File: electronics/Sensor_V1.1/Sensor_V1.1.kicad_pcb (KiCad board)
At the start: 2 copper layers, 45.9 x 25.6 mm, 55 parts, among them J1 nuclone_small_left, J2 nuclone_small_right, J5 DevBoardUartInput, Q1 BC846, U1 PPG_sensor, U2 reference_sot23-3, U3 MCP6541

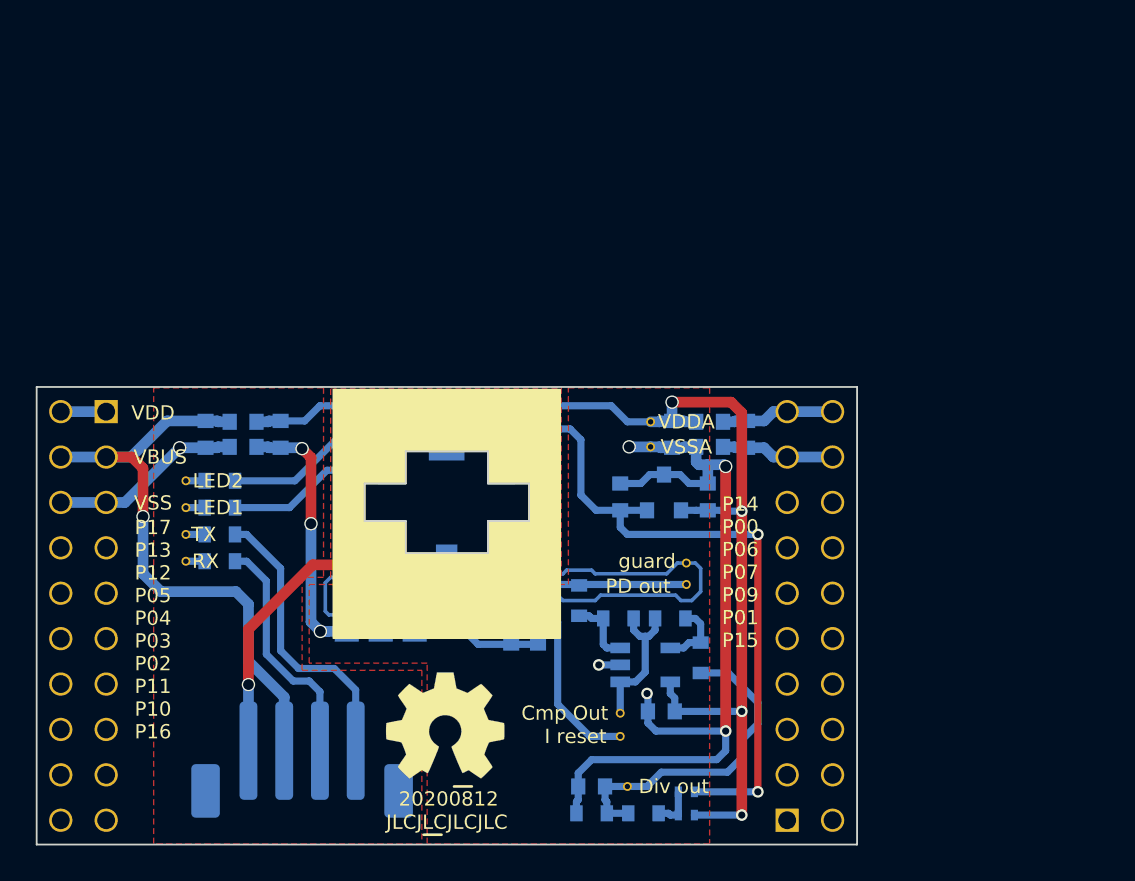
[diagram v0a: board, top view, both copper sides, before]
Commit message: minor layout changes and component swaps
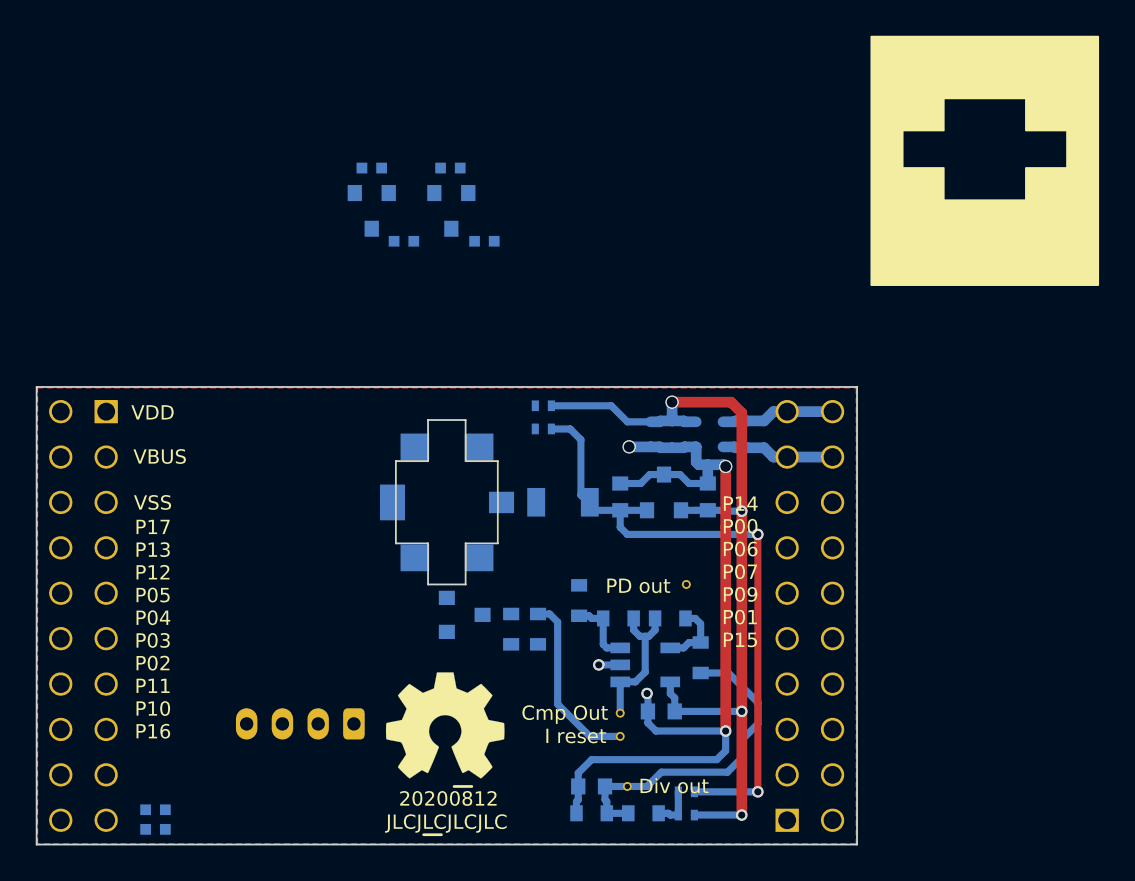
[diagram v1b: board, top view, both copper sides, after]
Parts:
- removed C1, C3: 1u, SquantorRcl:C_0603
- removed C2, C4: 10u, SquantorRcl:C_0603
- removed C7, C8: 4n7, SquantorRcl:C_0805+0603
- removed FB1, FB2, FB3, FB4: 600, SquantorRcl:L_0603
- removed JP2: bias VBUS, SquantorSpecial:solder_jumper_2way_noconn
- removed TP1: RX, SquantorTestPoints:TestPoint_hole_H03R05
- removed TP2: TX, SquantorTestPoints:TestPoint_hole_H03R05
- removed TP3: LED1, SquantorTestPoints:TestPoint_hole_H03R05
- removed TP4: LED2, SquantorTestPoints:TestPoint_hole_H03R05
- removed TP5, TP6: guard, SquantorTestPoints:TestPoint_pad_circle_D05
- removed TP7: VDDA, SquantorTestPoints:TestPoint_hole_H03R05
- removed TP8: VSSA, SquantorTestPoints:TestPoint_hole_H03R05
- removed TP9: guard, SquantorTestPoints:TestPoint_hole_H03R05
- added Q2: DMG1012, SquantorIC:SOT23-3, B.Cu at (80.9, 63.7)
- added Q3: DMG1012, SquantorIC:SOT23-3, B.Cu at (85.3, 63.7)
- added R5: 10K, SquantorRcl:R_0402_hand, B.Cu at (80.9, 61.3)
- added R6: 10K, SquantorRcl:R_0402_hand, B.Cu at (85.3, 61.3)
- C9: footprint SquantorRcl:C_0805+0603 -> SquantorRcl:C_1206
- J5: footprint Connector_JST:JST_PH_B4B-PH-SM4-TB_1x04-1MP_P2.00mm_Vertical -> Connector_JST:JST_PH_S4B-PH-K_1x04_P2.00mm_Horizontal
- R1, R2, R3, R4: footprint SquantorRcl:R_0603_hand -> SquantorRcl:R_0402_hand
- moved R4 20.0 mm to (87.2, 65.4)
- moved R3 18.1 mm to (82.7, 65.4)
- moved R2 15.8 mm to (68.8, 97.2)
- moved R1 15.4 mm to (68.8, 98.3)
- moved C9 10.4 mm to (91.6, 80.0), turned to 0 degrees
- moved J5 3.52 mm to (79.9, 92.4), turned to 180 degrees
- turned U1 to 0 degrees
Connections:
- net /GPIO_02 renamed Net-(J1-Pad9)
- net /GPIO_03 renamed Net-(J1-Pad10)
- net /GPIO_04 renamed Net-(J1-Pad11)
- net /GPIO_05 renamed Net-(J1-Pad12)
- net /GPIO_06 renamed Net-(J1-Pad13)
- net /GPIO_07 renamed Net-(J1-Pad14)
- net /GPIO_08 renamed Net-(J1-Pad15)
- net /GPIO_09 renamed Net-(J1-Pad16)
- net /GPIO_10 renamed Net-(J1-Pad17)
- net /GPIO_11 renamed Net-(J1-Pad18)
- net /GPIO_14 renamed Net-(J2-Pad1)
- net /GPIO_15 renamed Net-(J2-Pad2)
- net /GPIO_16 renamed Net-(J2-Pad3)
- net /GPIO_17 renamed Net-(J2-Pad4)
- net /GPIO_18 renamed Net-(J2-Pad5)
- net /GPIO_19 renamed Net-(J2-Pad6)
- net /GPIO_20 renamed Net-(J2-Pad7)
- net /GPIO_21 renamed Net-(J2-Pad8)
- net /GPIO_22 renamed Net-(J2-Pad9)
- net /GPIO_23 renamed Net-(J2-Pad10)
- net /GPIO_24 renamed Net-(J2-Pad11)
- net /GPIO_25 renamed Net-(J2-Pad12)
- net /GPIO_26 renamed Net-(J2-Pad13)
- net /GPIO_27 renamed Net-(J2-Pad14)
- net /GPIO_28 renamed Net-(J2-Pad15)
- net /GPIO_29 renamed Net-(J2-Pad16)
- C5 pad 1: /VDDA -> /VDD
- C5 pad 2: /VSSA -> /VSS
- C6 pad 2: /VSSA -> /VSS
- J1 pad 19: /GPIO_12 -> /UART_TX
- J1 pad 20: /GPIO_13 -> /UART_RX
- J1 pad 7: /GPIO_00 -> /LED1_EN
- J1 pad 8: /GPIO_01 -> /LED2_EN
- J2 pad 17: /VSSA_RAW -> /VSS
- J2 pad 18: /VSSA_RAW -> /VSS
- J2 pad 19: /VDDA_RAW -> /VDD
- J2 pad 20: /VDDA_RAW -> /VDD
- JP1 pad 1: /VDDA -> /VDD
- U1 pad 1: /LED1 -> /VDD
- U1 pad 3: /LED2 -> /VDD
- U1 pad 4: /VSS -> /LED2
- U1 pad 6: /VSS -> /LED1
- U2 pad 1: /VDDA -> /VDD
- U2 pad 3: /VSSA -> /VSS
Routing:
- net /PD_OUT_GUARD: track 45.2 -> 0.00 mm
- net /VBUS: track 34.2 -> 0.00 mm, vias 1 -> 0
- net /VSS: track 29.8 -> 6.37 mm, vias 4 -> 0
- net /PD_OUT: track 21.7 -> 0.00 mm
- net /VSSA: track 68.5 -> 47.1 mm, vias 9 -> 5
- net /LED2: track 18.3 -> 0.00 mm, vias 2 -> 0
- net Net-(J5-Pad4): track 16.4 -> 0.00 mm
- net Net-(J5-Pad3): track 13.5 -> 0.00 mm
- net /PD_BIAS: track 13.2 -> 0.00 mm
- net /LED1: track 9.61 -> 0.00 mm
- net /VSSA_RAW: track 6.37 -> 0.00 mm
- net /VDDA_RAW: track 6.37 -> 0.00 mm
- net Net-(Q1-Pad1): track 5.39 -> 0.00 mm
- net Net-(C4-Pad1): track 5.37 -> 0.00 mm
- net /VDD: track 2.54 -> 6.37 mm
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- removed copper zone on F.Cu, net /VSSA
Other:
- outline, holes or cut-outs redrawn

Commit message: updated versionnumber
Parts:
- N2: value 20200812 -> 20200908
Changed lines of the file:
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@@
       (effects (font (size 1 1) (thickness 0.15)))
     )
-    (fp_text value 20200812 (at 0.8 -0.1) (layer F.SilkS)
+    (fp_text value 20200908 (at 0.8 -0.1) (layer F.SilkS)
       (effects (font (size 0.8 0.8) (thickness 0.15)))
     )

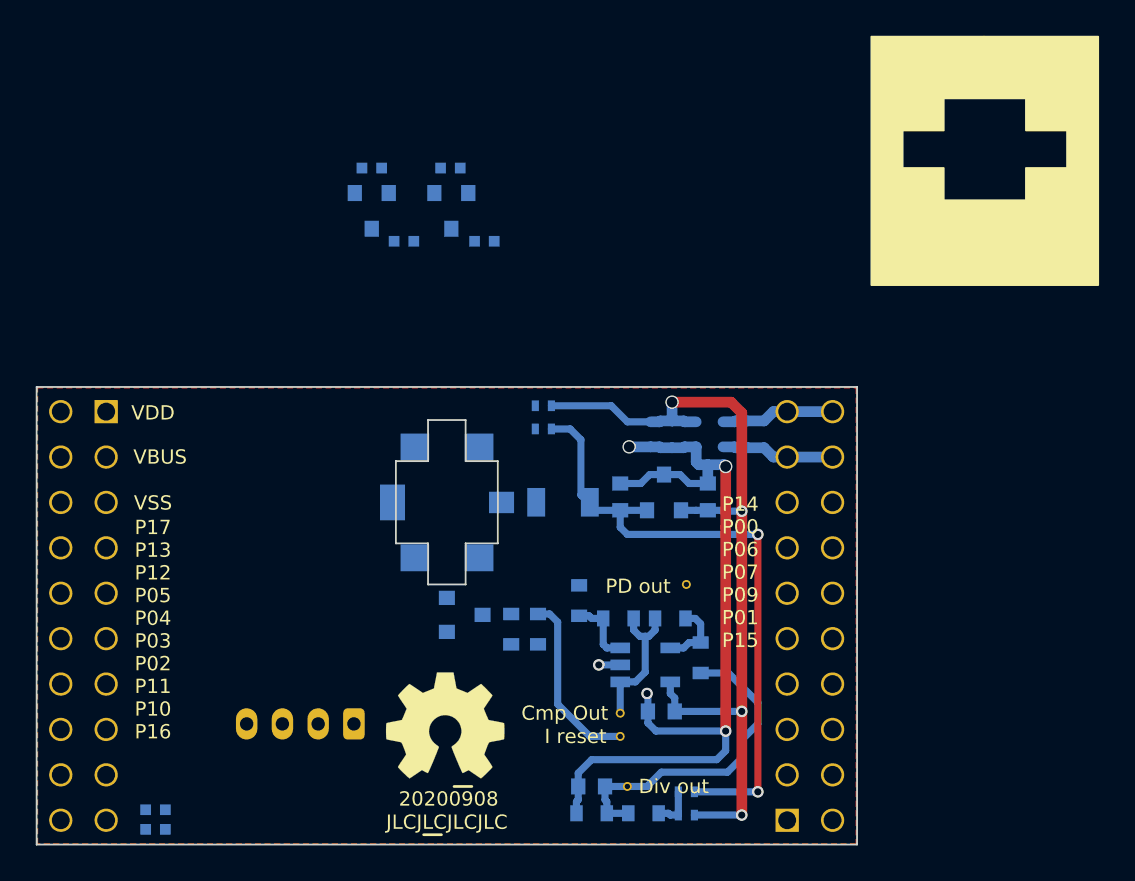
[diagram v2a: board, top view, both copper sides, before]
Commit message: placement and some routing of led drive circuitry
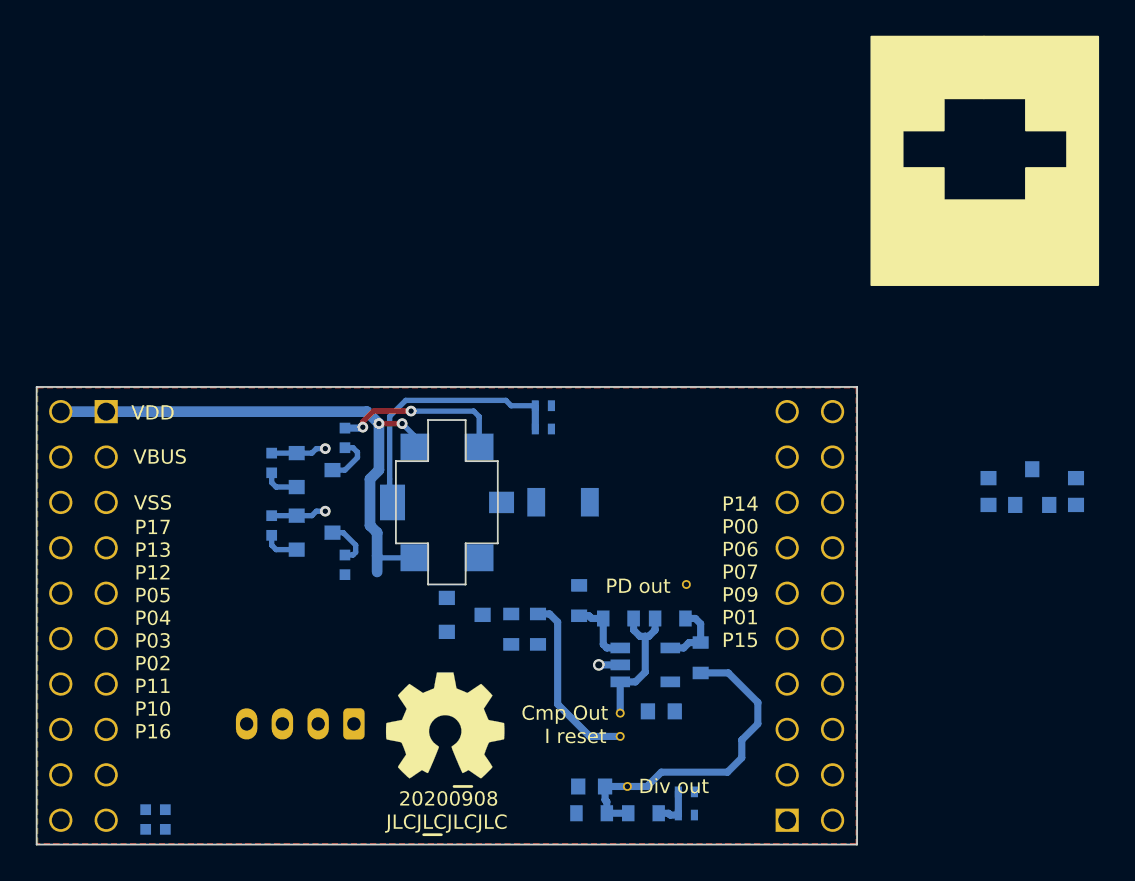
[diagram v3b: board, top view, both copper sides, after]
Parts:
- moved R5 20.8 mm to (75.3, 81.3), turned to 270 degrees
- moved C6 20.6 mm to (115.4, 79.4)
- moved C5 20.6 mm to (120.3, 79.4)
- moved U2 20.6 mm to (117.8, 79.2)
- moved R6 19.3 mm to (75.3, 77.8), turned to 270 degrees
- moved R3 18.4 mm to (79.4, 83.5), turned to 90 degrees
- moved Q2 18.3 mm to (77.7, 81.7), turned to 90 degrees
- moved Q3 16.4 mm to (77.7, 78.2), turned to 90 degrees
- moved R4 13.5 mm to (79.4, 76.4), turned to 270 degrees
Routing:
- net /VDDA: track 47.8 -> 0.00 mm, vias 4 -> 0
- net /VSSA: track 47.1 -> 1.20 mm, vias 5 -> 1
- net /VREF: track 35.8 -> 0.00 mm, vias 2 -> 0
- net /VDD: track 6.37 -> 31.8 mm, vias 0 -> 2
- net /PD_BIAS: track 0.00 -> 14.0 mm
- net /LED2: track 0.00 -> 9.91 mm, vias 0 -> 2
- net Net-(Q3-Pad3): track 0.00 -> 2.79 mm
- net Net-(Q2-Pad3): track 0.00 -> 2.65 mm
- net /LED2_EN: track 0.00 -> 2.05 mm
- net /LED1_EN: track 0.00 -> 2.05 mm
- net /VSS: track 6.37 -> 6.21 mm, vias 0 -> 2

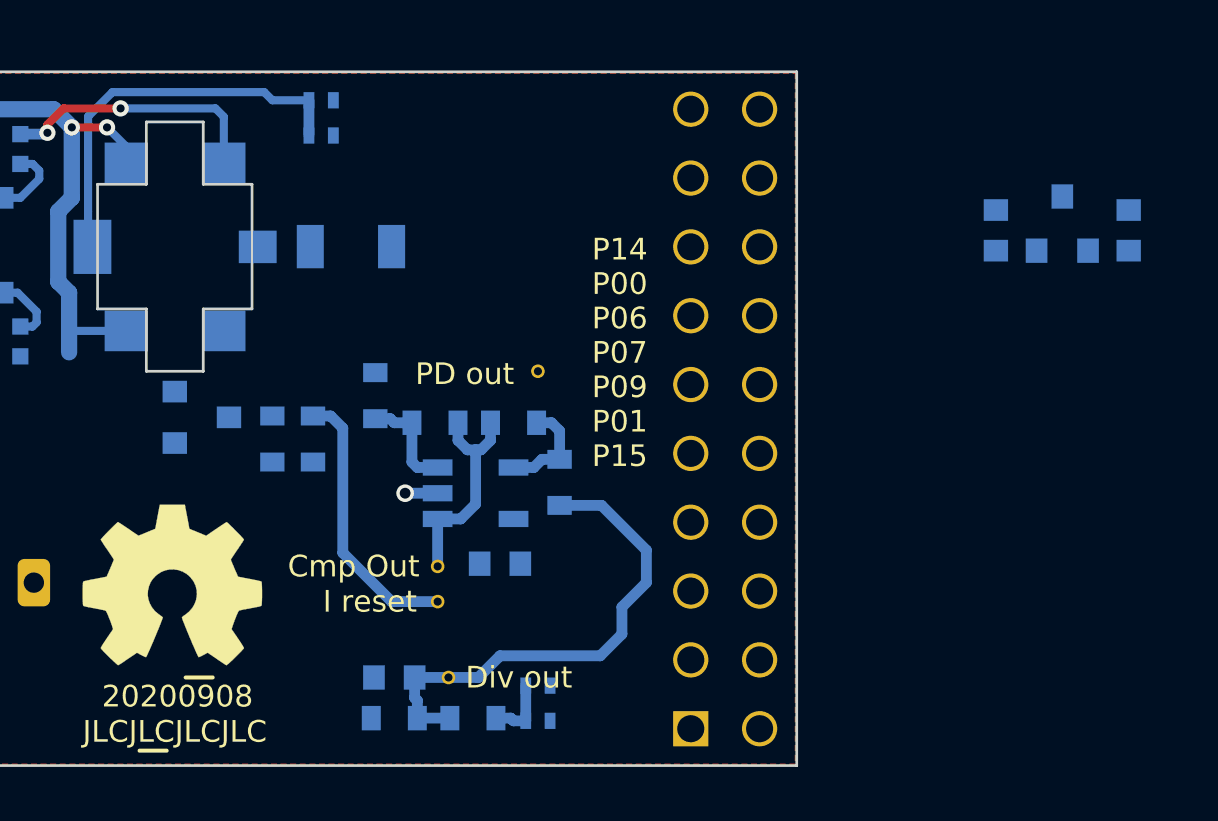
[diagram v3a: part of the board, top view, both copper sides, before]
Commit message: initial placement of some components
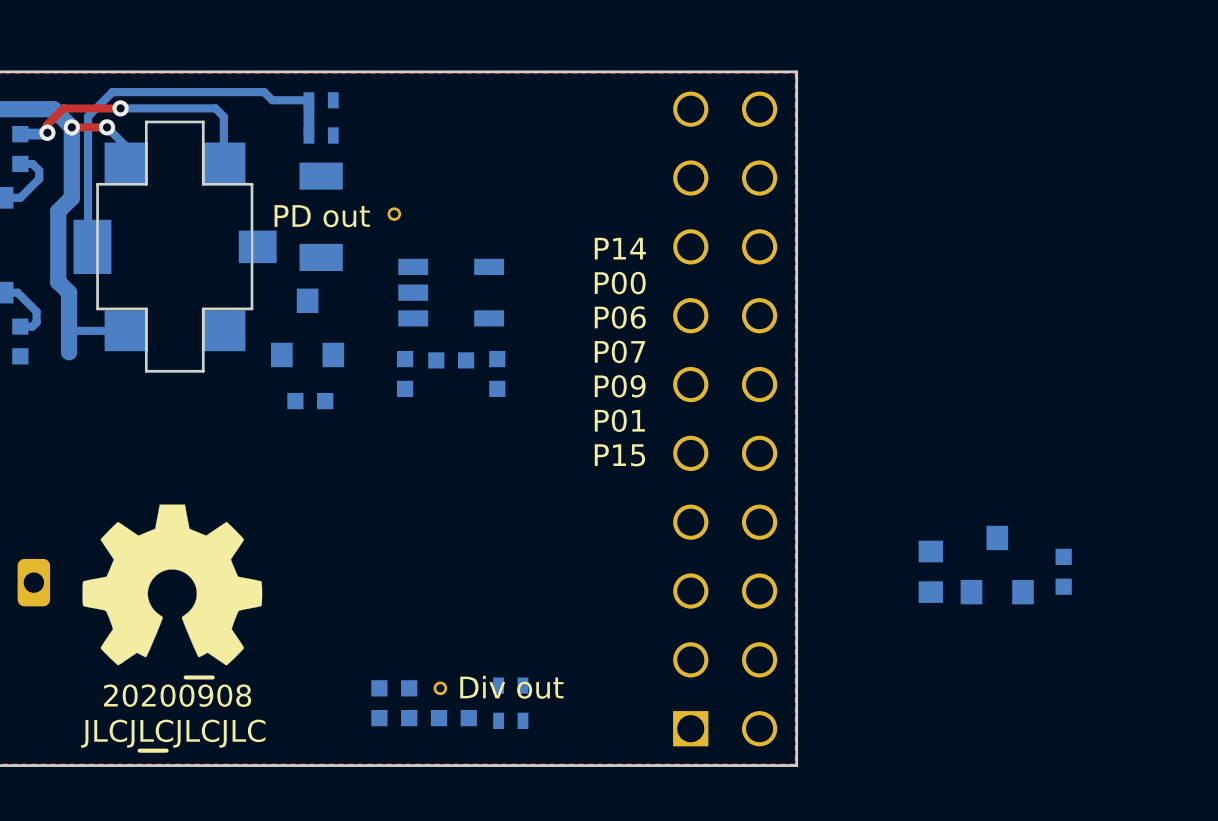
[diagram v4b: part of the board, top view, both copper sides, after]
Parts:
- removed R11: 4K7, SquantorRcl:R_0603_hand
- removed R15, R16: R, SquantorRcl:R_0603_hand
- removed TP12: I reset, SquantorTestPoints:TestPoint_hole_H03R05
- removed TP13: Cmp Out, SquantorTestPoints:TestPoint_hole_H03R05
- C10, C11, C5: footprint SquantorRcl:C_0603 -> SquantorRcl:C_0402
- Q1: value BC846 -> DMG1012
- R12, R17, R18, R7, R8: footprint SquantorRcl:R_0603_hand -> SquantorRcl:R_0402_hand
- moved C6 12.8 mm to (113.0, 92.0)
- moved C5 12.8 mm to (117.9, 92.0)
- moved U2 12.8 mm to (115.5, 91.8)
- moved TP10 7.86 mm to (93.2, 78.8)
- moved C10 7.71 mm to (95.3, 84.2)
- moved U3 7.45 mm to (95.3, 81.7)
- moved Q1 5.11 mm to (90.0, 83.0), turned to 180 degrees
- moved R18 4.61 mm to (97.0, 84.7)
- moved R17 4.39 mm to (93.6, 84.7), turned to 270 degrees
- moved R8 1.98 mm to (90.1, 85.7), turned to 0 degrees
- moved C9 1.56 mm to (90.5, 78.9), turned to 90 degrees
- moved JP4 1.00 mm to (97.5, 97.5)
- moved JP5 1.00 mm to (97.5, 96.2)
- moved R7 0.70 mm to (95.4, 97.4)
- moved TP11 0.50 mm to (94.9, 96.3)
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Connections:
- C9 pad 2: /VSSA -> /VSS_PD
- J1 pad 10: Net-(J1-Pad10) -> /I_reset
- Q1 pad 1: Net-(Q1-Pad1) -> /I_reset
- Q1 pad 2: /PD_OUT -> /VSS
- Q1 pad 3: /VSSA -> /PD_OUT
- R8 pad 1: /VSSA -> /VSS
- R8 pad 2: Net-(Q1-Pad1) -> /I_reset
- U3 pad 3: Net-(R15-Pad1) -> /PD_OUT
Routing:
- net /Divider_out: track 18.4 -> 0.00 mm
- net /I_reset: track 10.1 -> 0.00 mm
- net /CMP_OUT: track 8.17 -> 0.00 mm
- net Net-(R15-Pad1): track 3.89 -> 0.00 mm
- net Net-(R17-Pad2): track 3.85 -> 0.00 mm
- net Net-(JP4-Pad2): track 2.44 -> 0.00 mm
- net /VSSA: track 1.20 -> 0.00 mm, vias 1 -> 0

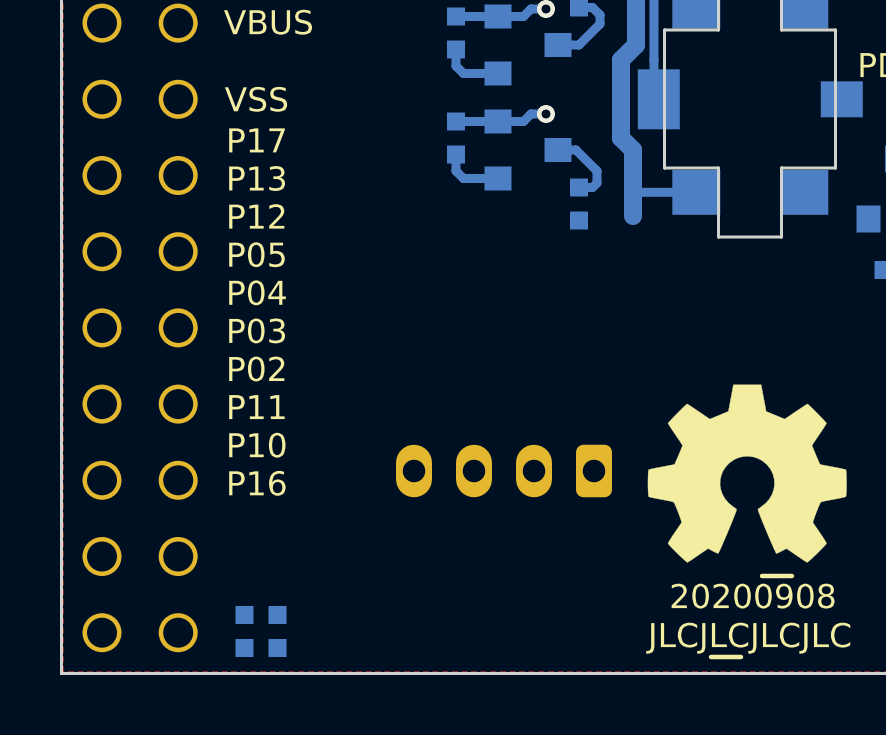
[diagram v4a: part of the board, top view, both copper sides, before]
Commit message: easier routing of UART pins
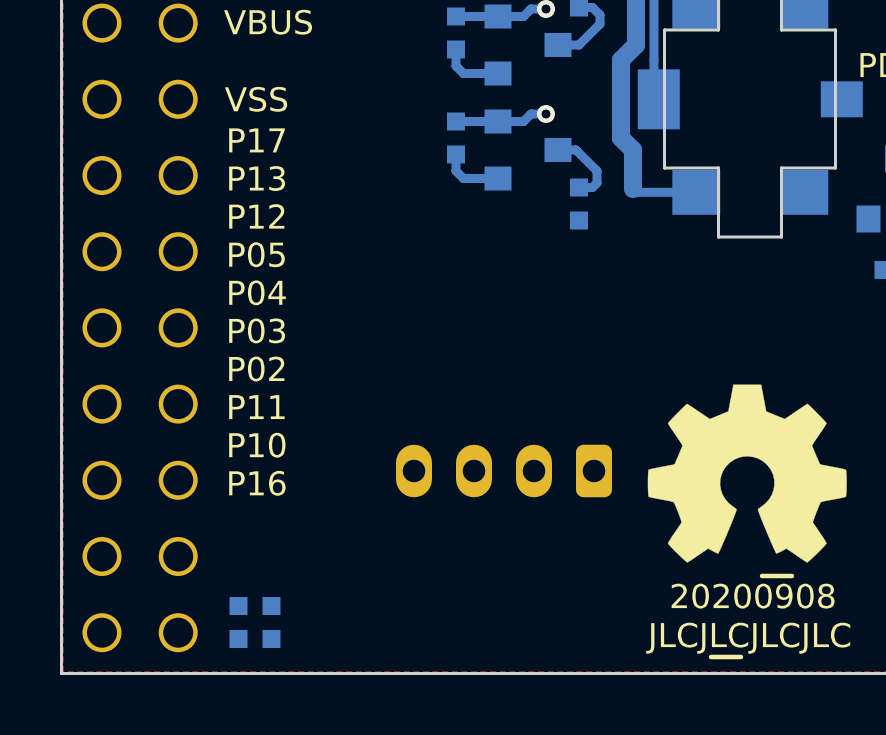
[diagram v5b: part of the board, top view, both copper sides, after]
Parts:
- moved R1 1.41 mm to (68.6, 96.9)
- moved R2 0.82 mm to (68.6, 98.0)
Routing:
- net /VDD: track 31.8 -> 30.9 mm
